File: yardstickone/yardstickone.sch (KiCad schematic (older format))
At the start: 67 parts, among them J1 USB-DEVICE, P1 EXPANSION, P2 BNC-CONN, P3 RESET_N, P4 DD, P5 DC, P6 3V3, P7 GND, T1 BALUN, U1 CC1111, U2 AP7313, U3 DMC2400, U4 RX_AMP, U5 SKY13385, U6 SKY13385, U7 TX_AMP, U8 DMC2400, X1 CRYSTAL

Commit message: changed from BNC to SMA connector
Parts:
- P2: value BNC-CONN -> SMA-EDGE; symbol BNC-CONN -> RF-CONN; Description CONN BNC RCPT JACK BOARD EDGE -> CONN SMA JACK 50 OHM EDGE MNT; Manufacturer Bomar -> Linx Technologies; Part Number 361V509E -> CONSMA003.062
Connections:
- wire segments 209 -> 236
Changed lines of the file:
@@
-EESchema Schematic File Version 2  date Sun Jan  6 11:43:45 2013
+EESchema Schematic File Version 2  date Sun 13 Apr 2014 12:09:50 PM MDT
 LIBS:power
 LIBS:device
@@
 Sheet 1 1
 Title ""
-Date "6 jan 2013"
+Date "13 apr 2014"
 Rev ""
 Comp ""
@@
 Connection ~ 11750 7200
 Wire Wire Line
-	11750 7100 11750 7300
+	11750 7100 11750 7200
+Wire Wire Line
+	11750 7200 11750 7300
 Wire Wire Line
 	12150 7800 12150 7700
-Wire Wire Line
-	14800 5650 14900 5650
-Wire Wire Line
-	14900 5650 14900 5850
 Wire Wire Line
 	7400 9250 7650 9250
@@
 Connection ~ 5200 9200
 Wire Wire Line
-	5200 8800 5200 9300
+	5200 8800 5200 9200
+Wire Wire Line
+	5200 9200 5200 9300
 Wire Wire Line
 	5200 9900 5200 9800
@@
 	10050 1050 10050 950
 Wire Wire Line
-	9750 950  9950 950
+	9750 950  9850 950
+Wire Wire Line
+	9850 950  9950 950
 Connection ~ 9850 950
 Wire Wire Line
-	9950 1850 9950 2150
+	9950 1850 9950 2050
+Wire Wire Line
+	9950 2050 9950 2150
 Wire Wire Line
 	9950 2750 9950 2650
 Wire Wire Line
-	10050 950  10650 950
+	10050 950  10450 950
+Wire Wire Line
+	10450 950  10650 950
 Connection ~ 10450 950
 Connection ~ 10900 6900
 Wire Wire Line
-	10500 6900 11100 6900
+	10500 6900 10900 6900
+Wire Wire Line
+	10900 6900 11100 6900
 Wire Wire Line
 	10400 8700 10400 8600
 Wire Wire Line
-	10400 7800 10400 8100
+	10400 7800 10400 8000
+Wire Wire Line
+	10400 8000 10400 8100
 Connection ~ 10300 6900
 Wire Wire Line
-	10200 6900 10400 6900
+	10200 6900 10300 6900
+Wire Wire Line
+	10300 6900 10400 6900
 Wire Wire Line
 	10500 6900 10500 7000
@@
 	10900 7500 10900 7400
 Wire Wire Line
-	11750 7800 11750 8000
+	11750 7800 11750 7900
+Wire Wire Line
+	11750 7900 11750 8000
 Wire Wire Line
 	13400 5450 13600 5450
@@
 Connection ~ 14100 5450
 Wire Wire Line
-	14000 5450 14200 5450
+	14000 5450 14100 5450
+Wire Wire Line
+	14100 5450 14200 5450
 Wire Wire Line
 	14100 6150 14100 6050
@@
 	3750 3750 4050 3750
 Wire Wire Line
-	3750 3450 3750 3750
+	3750 3450 3750 3550
+Wire Wire Line
+	3750 3550 3750 3750
 Wire Wire Line
 	3650 3550 3750 3550
@@
 	4750 5500 4750 5050
 Wire Wire Line
-	3950 5500 4750 5500
+	3950 5500 4350 5500
+Wire Wire Line
+	4350 5500 4750 5500
 Wire Wire Line
 	4050 6100 4050 6000
@@
 	4350 5600 4350 5500
 Wire Wire Line
-	2550 5400 3050 5400
+	2550 5400 2950 5400
+Wire Wire Line
+	2950 5400 3050 5400
 Wire Wire Line
 	2750 7550 2750 7450
@@
 	7150 3750 7150 3850
 Wire Wire Line
-	6050 3850 7250 3850
+	6050 3850 7150 3850
+Wire Wire Line
+	7150 3850 7250 3850
 Wire Wire Line
 	7150 3250 7150 3350
@@
 	7800 4450 7700 4450
 Wire Wire Line
-	7350 4250 7350 5250
+	7350 4250 7350 5150
+Wire Wire Line
+	7350 5150 7350 5250
 Wire Wire Line
 	7350 4250 6050 4250
@@
 Connection ~ 4850 5650
 Wire Wire Line
-	4850 5050 4850 5750
+	4850 5050 4850 5650
+Wire Wire Line
+	4850 5650 4850 5750
 Wire Wire Line
 	4750 5650 4850 5650
@@
 	6650 5150 6550 5150
 Wire Wire Line
-	6050 4450 6250 4450
+	6050 4450 6150 4450
+Wire Wire Line
+	6150 4450 6250 4450
 Wire Wire Line
 	7900 4100 7800 4100
@@
 	5350 3050 5350 2950
 Wire Wire Line
-	5350 2950 5650 2950
+	5350 2950 5450 2950
+Wire Wire Line
+	5450 2950 5550 2950
+Wire Wire Line
+	5550 2950 5650 2950
 Wire Wire Line
 	5550 2850 5550 2950
@@
 	6050 4350 6550 4350
 Wire Wire Line
-	6550 4350 6550 5250
-Wire Wire Line
-	7700 4150 7700 4550
+	6550 4350 6550 5150
+Wire Wire Line
+	6550 5150 6550 5250
+Wire Wire Line
+	7700 4150 7700 4450
+Wire Wire Line
+	7700 4450 7700 4550
 Wire Wire Line
 	7700 5050 7700 4950
 Wire Wire Line
-	6050 3750 6850 3750
-Wire Wire Line
-	3150 7050 3350 7050
+	6050 3750 6750 3750
+Wire Wire Line
+	6750 3750 6850 3750
+Wire Wire Line
+	3150 7050 3250 7050
+Wire Wire Line
+	3250 7050 3350 7050
 Connection ~ 3250 7050
 Wire Wire Line
@@
 Connection ~ 2750 6950
 Wire Wire Line
-	3550 5400 4650 5400
+	3550 5400 4050 5400
+Wire Wire Line
+	4050 5400 4650 5400
 Wire Wire Line
 	4650 5400 4650 5050
@@
 	5250 5550 5250 5050
 Wire Wire Line
-	4700 2400 5150 2400
+	4700 2400 5000 2400
+Wire Wire Line
+	5000 2400 5150 2400
 Connection ~ 5000 2400
 Wire Wire Line
@@
 	2650 5300 2550 5300
 Wire Wire Line
-	2400 6950 3350 6950
+	2400 6950 2650 6950
+Wire Wire Line
+	2650 6950 2750 6950
+Wire Wire Line
+	2750 6950 3350 6950
 Wire Wire Line
 	3850 4050 4050 4050
@@
 Connection ~ 10500 1950
 Wire Wire Line
-	10050 1950 10800 1950
-Wire Wire Line
-	11550 6400 12050 6400
+	10050 1950 10500 1950
+Wire Wire Line
+	10500 1950 10800 1950
+Wire Wire Line
+	11550 6400 11750 6400
+Wire Wire Line
+	11750 6400 12050 6400
 Wire Wire Line
 	10750 6400 10850 6400
@@
 Wire Wire Line
 	8550 9250 8450 9250
-Wire Wire Line
-	14800 5750 14900 5750
-Connection ~ 14900 5750
 Wire Wire Line
 	11750 7200 12150 7200
@@
 L GND #PWR02
 U 1 1 50A0885D
-P 14900 5850
-F 0 "#PWR02" H 14900 5850 30  0001 C CNN
-F 1 "GND" H 14900 5780 30  0001 C CNN
-	1    14900 5850
-	1    0    0    -1
-$EndComp
-$Comp
-L BNC-CONN P2
+P 14500 5950
+F 0 "#PWR02" H 14500 5950 30  0001 C CNN
+F 1 "GND" H 14500 5880 30  0001 C CNN
+	1    14500 5950
+	1    0    0    -1
+$EndComp
+$Comp
+L RF-CONN P2
 U 1 1 50A0883B
 P 14500 5450
 F 0 "P2" H 14500 5600 60  0000 C CNN
-F 1 "BNC-CONN" H 14500 5300 60  0000 C CNN
-F 4 "Bomar" H 14500 5450 60  0001 C CNN "Manufacturer"
-F 5 "361V509E" H 14500 5450 60  0001 C CNN "Part Number"
-F 6 "CONN BNC RCPT JACK BOARD EDGE" H 14500 5450 60  0001 C CNN "Description"
+F 1 "SMA-EDGE" H 14500 5300 60  0000 C CNN
+F 4 "Linx Technologies" H 14500 5450 60  0001 C CNN "Manufacturer"
+F 5 "CONSMA003.062" H 14500 5450 60  0001 C CNN "Part Number"
+F 6 "CONN SMA JACK 50 OHM EDGE MNT" H 14500 5450 60  0001 C CNN "Description"
 	1    14500 5450
 	-1   0    0    -1
@@
 Wire Wire Line
 	14200 3450 14200 3550
+Wire Wire Line
+	14500 5850 14500 5950
 $EndSCHEMATC

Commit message: reduced solder mask clearance and set paste clearance to 0 (OSH Stencils)
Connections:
- wire segments 236 -> 207
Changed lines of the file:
@@
-EESchema Schematic File Version 2  date Sun 13 Apr 2014 12:09:50 PM MDT
+EESchema Schematic File Version 2  date Sun 13 Apr 2014 01:16:34 PM MDT
 LIBS:power
 LIBS:device
@@
 Connection ~ 11750 7200
 Wire Wire Line
-	11750 7100 11750 7200
-Wire Wire Line
-	11750 7200 11750 7300
+	11750 7100 11750 7300
 Wire Wire Line
 	12150 7800 12150 7700
@@
 Connection ~ 5200 9200
 Wire Wire Line
-	5200 8800 5200 9200
-Wire Wire Line
-	5200 9200 5200 9300
+	5200 8800 5200 9300
 Wire Wire Line
 	5200 9900 5200 9800
@@
 	10050 1050 10050 950
 Wire Wire Line
-	9750 950  9850 950
-Wire Wire Line
-	9850 950  9950 950
+	9750 950  9950 950
 Connection ~ 9850 950
 Wire Wire Line
-	9950 1850 9950 2050
-Wire Wire Line
-	9950 2050 9950 2150
+	9950 1850 9950 2150
 Wire Wire Line
 	9950 2750 9950 2650
 Wire Wire Line
-	10050 950  10450 950
-Wire Wire Line
-	10450 950  10650 950
+	10050 950  10650 950
 Connection ~ 10450 950
 Connection ~ 10900 6900
 Wire Wire Line
-	10500 6900 10900 6900
-Wire Wire Line
-	10900 6900 11100 6900
+	10500 6900 11100 6900
 Wire Wire Line
 	10400 8700 10400 8600
 Wire Wire Line
-	10400 7800 10400 8000
-Wire Wire Line
-	10400 8000 10400 8100
+	10400 7800 10400 8100
 Connection ~ 10300 6900
 Wire Wire Line
-	10200 6900 10300 6900
-Wire Wire Line
-	10300 6900 10400 6900
+	10200 6900 10400 6900
 Wire Wire Line
 	10500 6900 10500 7000
@@
 	10900 7500 10900 7400
 Wire Wire Line
-	11750 7800 11750 7900
-Wire Wire Line
-	11750 7900 11750 8000
+	11750 7800 11750 8000
 Wire Wire Line
 	13400 5450 13600 5450
@@
 Connection ~ 14100 5450
 Wire Wire Line
-	14000 5450 14100 5450
-Wire Wire Line
-	14100 5450 14200 5450
+	14000 5450 14200 5450
 Wire Wire Line
 	14100 6150 14100 6050
@@
 	3750 3750 4050 3750
 Wire Wire Line
-	3750 3450 3750 3550
-Wire Wire Line
-	3750 3550 3750 3750
+	3750 3450 3750 3750
 Wire Wire Line
 	3650 3550 3750 3550
@@
 	4750 5500 4750 5050
 Wire Wire Line
-	3950 5500 4350 5500
-Wire Wire Line
-	4350 5500 4750 5500
+	3950 5500 4750 5500
 Wire Wire Line
 	4050 6100 4050 6000
@@
 	4350 5600 4350 5500
 Wire Wire Line
-	2550 5400 2950 5400
-Wire Wire Line
-	2950 5400 3050 5400
+	2550 5400 3050 5400
 Wire Wire Line
 	2750 7550 2750 7450
@@
 	7150 3750 7150 3850
 Wire Wire Line
-	6050 3850 7150 3850
-Wire Wire Line
-	7150 3850 7250 3850
+	6050 3850 7250 3850
 Wire Wire Line
 	7150 3250 7150 3350
@@
 	7800 4450 7700 4450
 Wire Wire Line
-	7350 4250 7350 5150
-Wire Wire Line
-	7350 5150 7350 5250
+	7350 4250 7350 5250
 Wire Wire Line
 	7350 4250 6050 4250
@@
 Connection ~ 4850 5650
 Wire Wire Line
-	4850 5050 4850 5650
-Wire Wire Line
-	4850 5650 4850 5750
+	4850 5050 4850 5750
 Wire Wire Line
 	4750 5650 4850 5650
@@
 	6650 5150 6550 5150
 Wire Wire Line
-	6050 4450 6150 4450
-Wire Wire Line
-	6150 4450 6250 4450
+	6050 4450 6250 4450
 Wire Wire Line
 	7900 4100 7800 4100
@@
 	5350 3050 5350 2950
 Wire Wire Line
-	5350 2950 5450 2950
-Wire Wire Line
-	5450 2950 5550 2950
-Wire Wire Line
-	5550 2950 5650 2950
+	5350 2950 5650 2950
 Wire Wire Line
 	5550 2850 5550 2950
@@
 	6050 4350 6550 4350
 Wire Wire Line
-	6550 4350 6550 5150
-Wire Wire Line
-	6550 5150 6550 5250
-Wire Wire Line
-	7700 4150 7700 4450
-Wire Wire Line
-	7700 4450 7700 4550
+	6550 4350 6550 5250
+Wire Wire Line
+	7700 4150 7700 4550
 Wire Wire Line
 	7700 5050 7700 4950
 Wire Wire Line
-	6050 3750 6750 3750
-Wire Wire Line
-	6750 3750 6850 3750
-Wire Wire Line
-	3150 7050 3250 7050
-Wire Wire Line
-	3250 7050 3350 7050
+	6050 3750 6850 3750
+Wire Wire Line
+	3150 7050 3350 7050
 Connection ~ 3250 7050
 Wire Wire Line
@@
 Connection ~ 2750 6950
 Wire Wire Line
-	3550 5400 4050 5400
-Wire Wire Line
-	4050 5400 4650 5400
+	3550 5400 4650 5400
 Wire Wire Line
 	4650 5400 4650 5050
@@
 	5250 5550 5250 5050
 Wire Wire Line
-	4700 2400 5000 2400
-Wire Wire Line
-	5000 2400 5150 2400
+	4700 2400 5150 2400
 Connection ~ 5000 2400
 Wire Wire Line
@@
 	2650 5300 2550 5300
 Wire Wire Line
-	2400 6950 2650 6950
-Wire Wire Line
-	2650 6950 2750 6950
-Wire Wire Line
-	2750 6950 3350 6950
+	2400 6950 3350 6950
 Wire Wire Line
 	3850 4050 4050 4050
@@
 Connection ~ 10500 1950
 Wire Wire Line
-	10050 1950 10500 1950
-Wire Wire Line
-	10500 1950 10800 1950
-Wire Wire Line
-	11550 6400 11750 6400
-Wire Wire Line
-	11750 6400 12050 6400
+	10050 1950 10800 1950
+Wire Wire Line
+	11550 6400 12050 6400
 Wire Wire Line
 	10750 6400 10850 6400

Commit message: added programming pins to expansion header, made compatible with GoodFET pinout
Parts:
- removed P1: EXPANSION, symbol CONN_5X2
- added P1: CONN_02X07, cc1111-legacy:GSG-HEADER-2x7, symbol CONN_02X07
- C1, C12, C13, C15, C16, C17, C24, L1, R10, R11, R12, R5, R8, R9: footprint (none) -> cc1111-legacy:GSG-0603
- C10, C11, C14, C18, C19, C2, C20, C21, C22, C23, C25, C26, C27, C28, C3, C4, C5, C6, C7, C8, C9, D1, R1, R14, R15, R2, R3, R4, R6, R7: footprint (none) -> cc1111-legacy:GSG-0402
- D2, D3, D4: footprint (none) -> cc1111-legacy:GSG-0603D
- FB1: footprint (none) -> cc1111-legacy:GSG-0805
- J1: footprint (none) -> cc1111-legacy:GSG-USB-A-1001-010-01001-SHIELD
- P2: footprint (none) -> cc1111-legacy:GSG-SMA-EDGE
- P3, P4, P5, P6, P7: footprint (none) -> cc1111-legacy:GSG-TESTPOINT-100MIL
- R13: footprint (none) -> cc1111-legacy:GSG-0603-SHORT-10MIL
- T1: footprint (none) -> cc1111-legacy:GSG-B0310J50100AHF
- U1: footprint (none) -> cc1111-legacy:GSG-QFN36
- U2: footprint (none) -> cc1111-legacy:GSG-SOT23-3
- U3, U8: footprint (none) -> cc1111-legacy:GSG-SOT563
- U4: footprint (none) -> cc1111-legacy:GSG-SOT363
- U5, U6: footprint (none) -> cc1111-legacy:GSG-SKY13385
- U7: footprint (none) -> cc1111-legacy:GSG-SOT343
- X1: footprint (none) -> cc1111-legacy:GSG-XTAL-TXC-7A
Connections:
- wire segments 207 -> 211

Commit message: replaced TX amp with SPF5043Z
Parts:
- R7: value 15 -> 0; Description RES 15 OHM 1/16W 1% 0402 SMD -> (none); Manufacturer Stackpole -> (none); Note 1% -> (none); Part Number RMCF0402FT15R0 -> (none)
- U7: Description IC AMP MMIC 80MA 4.5V SOT343 -> IC MMIC AMP LN 50-4000MHZ SOT343; Manufacturer Infineon -> RFMD; Part Number BGA 616 H6327 -> SPF5043Z
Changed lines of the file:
@@
 F 2 "cc1111-legacy:GSG-SOT343" H 11200 6350 60  0001 C CNN
 F 3 "" H 11200 6350 60  0001 C CNN
-F 4 "Infineon" H 11200 6350 60  0001 C CNN "Manufacturer"
-F 5 "BGA 616 H6327" H 11200 6350 60  0001 C CNN "Part Number"
-F 6 "IC AMP MMIC 80MA 4.5V SOT343" H 11200 6350 60  0001 C CNN "Description"
+F 4 "RFMD" H 11200 6350 60  0001 C CNN "Manufacturer"
+F 5 "SPF5043Z" H 11200 6350 60  0001 C CNN "Part Number"
+F 6 "IC MMIC AMP LN 50-4000MHZ SOT343" H 11200 6350 60  0001 C CNN "Description"
 	1    11200 6350
 	1    0    0    -1
@@
 	1    11750 8500
 	1    0    0    -1
-$EndComp
-$Comp
-L R R7
-U 1 1 50A02E3C
-P 11750 7550
-F 0 "R7" V 11830 7550 50  0000 C CNN
-F 1 "15" V 11750 7550 50  0000 C CNN
-F 2 "cc1111-legacy:GSG-0402" H 11750 7550 60  0001 C CNN
-F 3 "" H 11750 7550 60  0001 C CNN
-F 4 "Stackpole" H 11750 7550 60  0001 C CNN "Manufacturer"
-F 5 "RMCF0402FT15R0" H 11750 7550 60  0001 C CNN "Part Number"
-F 6 "RES 15 OHM 1/16W 1% 0402 SMD" H 11750 7550 60  0001 C CNN "Description"
-F 7 "1%" V 11650 7550 60  0000 C CNN "Note"
-	1    11750 7550
-	-1   0    0    1
 $EndComp
 $Comp
@@
 Wire Wire Line
 	7800 9300 7800 9600
+$Comp
+L R R7
+U 1 1 5494B37F
+P 11750 7550
+F 0 "R7" V 11830 7550 50  0000 C CNN
+F 1 "0" V 11750 7550 50  0000 C CNN
+F 2 "cc1111-legacy:GSG-0402" H 11750 7550 60  0001 C CNN
+F 3 "" H 11750 7550 60  0001 C CNN
+	1    11750 7550
+	-1   0    0    1
+$EndComp
 $EndSCHEMATC

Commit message: corrected TX amp orientation
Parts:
- U7: symbol BGA616 -> SPF5043Z
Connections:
- net at C23.1, L1.1: now also U7.1 (OUT); no longer U7.3 (OUT)
- net at C22.2: now also U7.3 (IN); no longer U7.1 (IN)
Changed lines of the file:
@@
 $EndComp
 $Comp
-L BGA616 U7
+L SPF5043Z U7
 U 1 1 50A05129
 P 11200 6350
@@
 F 6 "IC MMIC AMP LN 50-4000MHZ SOT343" H 11200 6350 60  0001 C CNN "Description"
 	1    11200 6350
-	1    0    0    -1
+	-1   0    0    1
 $EndComp
 $Comp

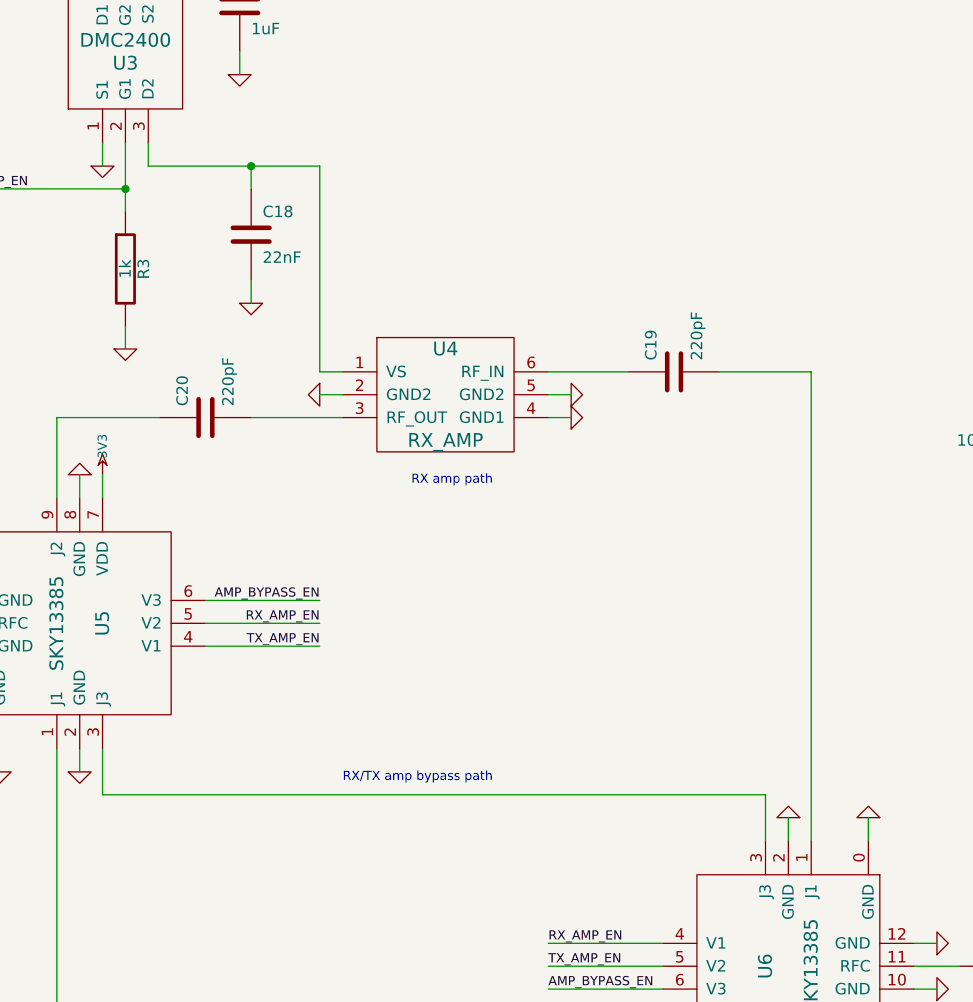
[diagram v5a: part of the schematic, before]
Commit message: replaced RX amp with BGA420
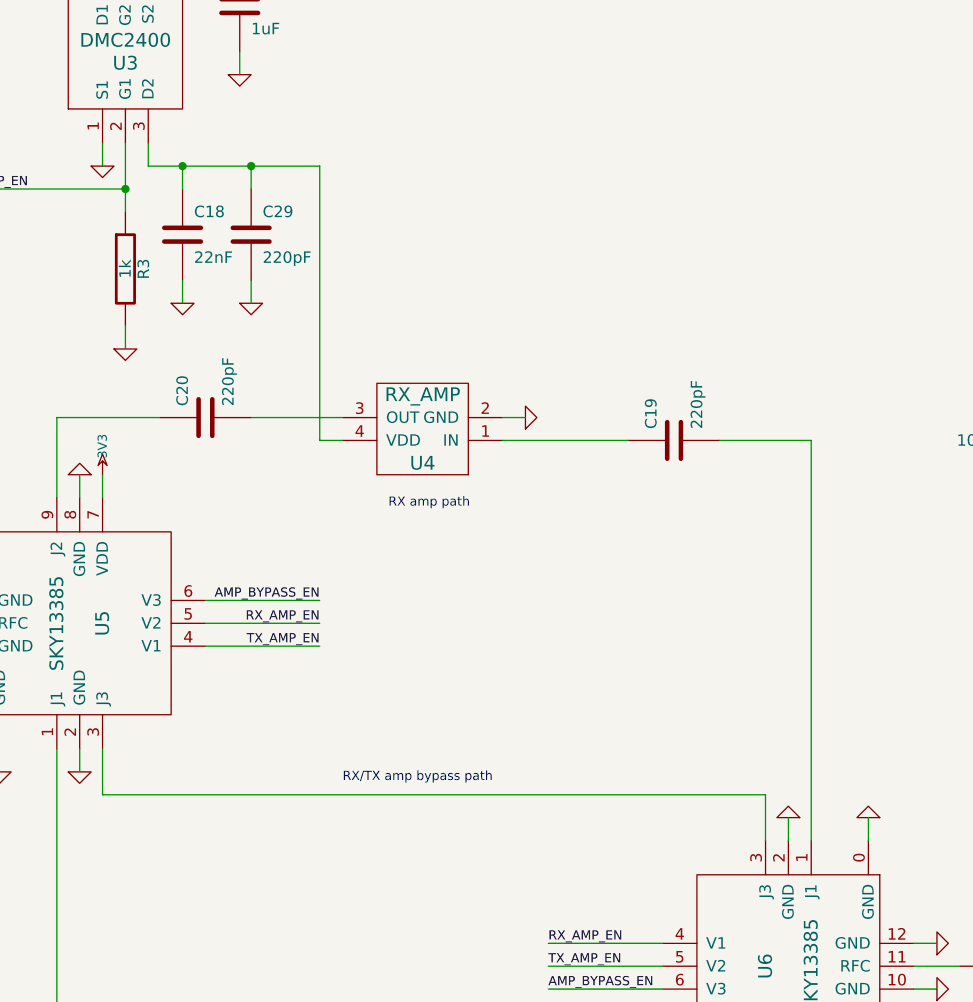
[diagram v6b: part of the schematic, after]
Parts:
- removed U4: RX_AMP, cc1111-legacy:GSG-SOT363, symbol BGA2717
- added C29: 220pF, cc1111-legacy:GSG-0402, symbol C
- added U4: RX_AMP, symbol BGA420
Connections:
- net GND: now also C29.2, U4.2 (GND)
- net at C18.1, U3.3 (D2): now also C29.1, U4.4 (VDD)
- net at C20.2: now also U4.3 (OUT)
- net at C19.1: now also U4.1 (IN)
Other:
- moved on the sheet: C18, C19

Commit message: rotated RX amp
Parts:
- U4: footprint (none) -> cc1111-legacy:GSG-SOT343
